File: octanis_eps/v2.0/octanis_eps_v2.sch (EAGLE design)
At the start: 186 parts, among them Q1 CSD16327Q3_DQG_8, Q2 CSD16327Q3_DQG_8, Q3 CSD16327Q3_DQG_8, Q4 BSS123, Q5 CSD16327Q3_DQG_8, Q6 CSD16327Q3_DQG_8, Q7 BSC0901NS, U1 MSP430FR5969, U10 INA213, U11 MIC5019, U12 TPS61088, U13 TPS61232, U15 Value, U16 Value, U17 Value, U2 OPA2333DGK, U3 TPS2022D, U4 TPS2022D, U5 BQ24650_RVA_16, U7 TPS61232, U9 INA213, X1 32.768kHz

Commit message: EPS v2.0 finished routing
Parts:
- removed VCC_GND: (no value), Headerlibrary:PINHD-1X2
- added JP7: (no value), Headerlibrary:PINHD-1X16
- added U$2: UX60SC-MB-5ST, usbminib:UX60SC-MB-5ST
- C31, C47: device rcl:C-EUC0603 -> resistor:C-EUC0805
- JP4: device pinhead:PINHD-2X10 -> Headerlibrary:PINHD-1X6
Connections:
- net +12V: now also JP7.14; no longer JP4.4
- net +3V3: now also JP7.2; no longer VCC_GND.1
- net +3V3_1: now also JP7.6; no longer JP4.12
- net +3V3_2: now also JP7.8; no longer JP4.14
- net +3V3_M: now also JP7.4; no longer JP4.10
- net +5V_1: now also JP7.10; no longer JP4.6
- net +5V_2: now also JP7.12; no longer JP4.8
- net BAT_OUT: now also JP4.1, JP4.3, JP4.5; no longer JP4.15, JP4.17, JP4.19
- net DIRECT: now also JP7.16; no longer JP4.2
- net GND: now also JP7.1, JP7.11, JP7.13, JP7.15, JP7.3, JP7.5, JP7.7, JP7.9, U$2.5; no longer JP4.1, JP4.11, JP4.13, JP4.3, JP4.5, JP4.7, JP4.9, VCC_GND.2
- net HEAT1: now also JP4.6; no longer JP4.16
- net HEAT2: now also JP4.4; no longer JP4.18
- net HEAT3: now also JP4.2; no longer JP4.20
- net V_USB: now also U$2.1
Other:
- moved on the sheet: C31, C47

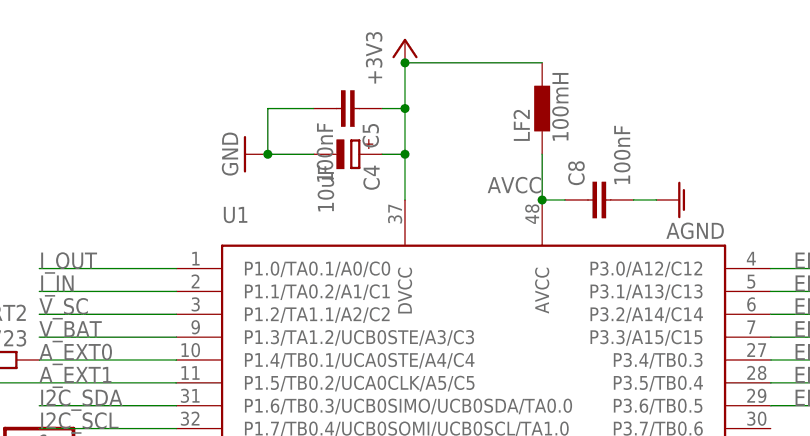
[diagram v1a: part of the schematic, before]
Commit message: performed DRC
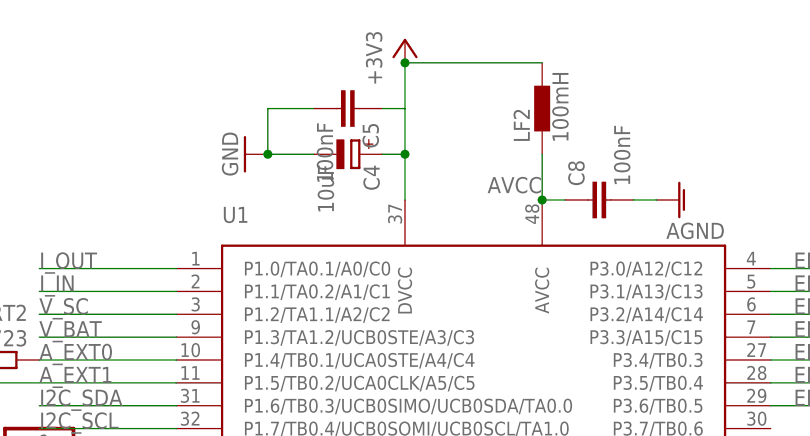
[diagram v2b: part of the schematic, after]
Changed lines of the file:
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@@
 <segment>
 <pinref part="+3V8" gate="G$1" pin="+3V3"/>
-<pinref part="U1" gate="G$1" pin="DVCC"/>
 <wire x1="91.44" y1="307.34" x2="91.44" y2="302.26" width="0.1524" layer="91"/>
 <pinref part="LF2" gate="G$1" pin="2"/>
-<wire x1="91.44" y1="302.26" x2="91.44" y2="297.18" width="0.1524" layer="91"/>
-<wire x1="91.44" y1="297.18" x2="91.44" y2="292.1" width="0.1524" layer="91"/>
 <wire x1="91.44" y1="307.34" x2="106.68" y2="307.34" width="0.1524" layer="91"/>
 <pinref part="C5" gate="G$1" pin="1"/>
 <wire x1="88.9" y1="302.26" x2="91.44" y2="302.26" width="0.1524" layer="91"/>
+<junction x="91.44" y="307.34"/>
+<pinref part="U1" gate="G$1" pin="DVCC"/>
+<wire x1="91.44" y1="292.1" x2="91.44" y2="297.18" width="0.1524" layer="91"/>
 <pinref part="C4" gate="G$1" pin="+"/>
+<wire x1="91.44" y1="297.18" x2="91.44" y2="302.26" width="0.1524" layer="91"/>
 <wire x1="88.9" y1="297.18" x2="91.44" y2="297.18" width="0.1524" layer="91"/>
-<junction x="91.44" y="302.26"/>
-<junction x="91.44" y="307.34"/>
+<junction x="91.44" y="297.18"/>
 </segment>
 <segment>
@@
 <pinref part="C8" gate="G$1" pin="1"/>
 <junction x="106.68" y="292.1"/>
-<junction x="91.44" y="297.18"/>
 <wire x1="109.22" y1="292.1" x2="106.68" y2="292.1" width="0.1524" layer="91"/>
 <label x="106.68" y="294.64" size="1.778" layer="95" rot="R180"/>

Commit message: corrected some GND mistakes; finished v2.0 silk layer
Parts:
- removed J1, J2, J3, J4: (no value), jumper:SJ
- removed RS3: 10m, Octanis1_EPS:CURRENT_RESISTOR
- removed U$1: MCP73831/2, Octanis1_EPS:MCP73831/2
- removed U16: Value, octanis_eps_v05:TPS630250RNCR
- added J108, J109, J110, J111: (no value), jumper:SJ
- added RS2: 10m, Octanis1_EPS:CURRENT_RESISTOR
- added U14: MIC5019, Octanis1_EPS:MIC5019
- added U8: TPS61232, texasinstruments:TPS61232
- C10, C9: value 1.5uF -> 22uF; device rcl:C-EUC0603 -> resistor:C-EUC0805
- C13: value 10uF -> 22uF
- C15: value 22uF -> 10nF; device resistor:C-EUC0805 -> rcl:C-EUC0603
- C16, C18: value 1uF -> 22uF; device rcl:C-EUC0603 -> resistor:C-EUC0805
- C17, C32: value 100nF -> 22uF; device rcl:C-EUC0603 -> resistor:C-EUC0805
- C19: value 10uF -> 10nF; device resistor:C-EUC0805 -> rcl:C-EUC0603
- C20: value 10nF -> 22uF; device rcl:C-EUC0603 -> resistor:C-EUC0805
- C23: value 10uF -> 1uF; device resistor:C-EUC0805 -> rcl:C-EUC0603
- C24, C47: value 22uF -> 100nF; device resistor:C-EUC0805 -> rcl:C-EUC0603
- C25, C39: value 22uF -> 1uF; device resistor:C-EUC0805 -> rcl:C-EUC0603
- C26: value 22uF -> 1.5uF; device resistor:C-EUC0805 -> rcl:C-EUC0603
- C27: value 2.2uF -> 1.5uF
- C28: value 1uF -> 10uF; device rcl:C-EUC0603 -> resistor:C-EUC0805
- C29, C45: value 100nF -> 10uF; device rcl:C-EUC0603 -> resistor:C-EUC0805
- C30: value 22pF -> 10uF; device rcl:C-EUC0603 -> resistor:C-EUC0805
- C34: value 1uF -> 100nF
- C35: value 150pF -> 1uF
- C36: value 22uF -> 22pF; device resistor:C-EUC0805 -> rcl:C-EUC0603
- C37: value 4.7nF -> 10uF; device rcl:C-EUC0603 -> resistor:C-EUC0805
- C38: value 22uF -> 2.2uF; device resistor:C-EUC0805 -> rcl:C-EUC0603
- C40: value 10uF -> 150pF; device resistor:C-EUC0805 -> rcl:C-EUC0603
- C41: value 10uF -> 4.7nF; device resistor:C-EUC0805 -> rcl:C-EUC0603
- C43: value 47uF Tantal -> 10uF; device rcl:C-EUC1210 -> resistor:C-EUC0805
- C44: value 10uF -> 47uF Tantal; device resistor:C-EUC0805 -> rcl:C-EUC1210
- C46: value 47nF -> 100nF
- C48: value 10nF -> 47nF
- JP3: device Headerlibrary:PINHD-1X2 -> Headerlibrary:PINHD-1X16
- JP4: device Headerlibrary:PINHD-1X6 -> Headerlibrary:PINHD-1X2
- JP7: device Headerlibrary:PINHD-1X16 -> Headerlibrary:PINHD-1X6
- L4: value DR127_6u8 -> 1uH; device inductors:DR127 -> Coilcraft:XFL4020
- L6: value 1.5uH -> DR127_6u8; device Coilcraft:XFL4020 -> inductors:DR127
- L7: value 1uH -> 1.5uH
- Q1: value CSD16327Q3_DQG_8 -> BSS123; device texasinstruments:CSD16327Q3_DQG_8 -> transistor-small-signal:BSS123
- Q4: value BSS123 -> CSD16327Q3_DQG_8; device transistor-small-signal:BSS123 -> texasinstruments:CSD16327Q3_DQG_8
- Q6: value CSD16327Q3_DQG_8 -> BSC0901NS; device texasinstruments:CSD16327Q3_DQG_8 -> transistor-power:BSC340N08NS3G
- Q7: value BSC0901NS -> CSD16327Q3_DQG_8; device transistor-power:BSC340N08NS3G -> texasinstruments:CSD16327Q3_DQG_8
- R13, R16: value 1k -> 1.5k
- R17, R19: value 1M -> 100k (0.1%)
- R18: value 1k -> 200k (0.1%)
- R20, R7: value 1k -> 330k (0.1%)
- R21: value 1M -> 150k
- R22, R24: value 1k -> 360k
- R23: value 200k (0.1%) -> 150k
- R25: value 330k (0.1%) -> 150k
- R26: value 1M -> 360k; device resistor:R-EU_R0603 -> rcl:R-EU_R0603
- R27, R53: device resistor:R-EU_R0603 -> rcl:R-EU_R0603
- R28: value dnp -> 1M
- R29: value Rmpph -> 1M
- R30: value 4k7 -> 1M
- R31: value 4k7 -> dnp
- R32: value 1M -> Rmpph
- R33: value Rmppl -> 4k7
- R34: value 100k (1%) -> 4k7
- R35: value 100k (1%) -> 1M
- R36: value 1M -> Rmppl
- R37: value 1M -> 100k (1%)
- R38: value 1M -> 1k; device resistor:R-EU_R0603 -> rcl:R-EU_R0603
- R39: value 2 -> 100k (1%); device rcl:R-EU_R2010 -> rcl:R-EU_R0603
- R4: value 100k (0.1%) -> 1k
- R40: value 10 -> 1k; device rcl:R-EU_R1206 -> rcl:R-EU_R0603
- R41: value 2.2M (1%) -> 1M; device rcl:R-EU_R0603 -> resistor:R-EU_R0603
- R42: device rcl:R-EU_R0603 -> resistor:R-EU_R0603
- R43: value 47k -> 1M
- R44: value 100k -> 2; device resistor:R-EU_R0603 -> rcl:R-EU_R2010
- R45: value 150-220k -> 10; device resistor:R-EU_R0603 -> rcl:R-EU_R1206
- R46: value 56k -> 2.2M (1%); device resistor:R-EU_R0603 -> rcl:R-EU_R0603
- R47: value 430k -> 2k; device resistor:R-EU_R0603 -> rcl:R-EU_R0603
- R48: value dnp -> 470; device resistor:R-EU_R0603 -> rcl:R-EU_R0603
- R49: value 1.5k -> 1k
- R50: value 1M -> 1k
- R52: value 2k -> 1k
- R54: value 470 -> 1k
- R55: value 150k -> 1M
- R56: value 360k -> 1M
- R57: value 360k -> 47k; device rcl:R-EU_R0603 -> resistor:R-EU_R0603
- R58: value 360k -> 100k; device rcl:R-EU_R0603 -> resistor:R-EU_R0603
- R59: value 150k -> 150-220k; device rcl:R-EU_R0603 -> resistor:R-EU_R0603
- R60: value 150k -> 56k; device rcl:R-EU_R0603 -> resistor:R-EU_R0603
- R61: value 1.5k -> 430k; device rcl:R-EU_R0603 -> resistor:R-EU_R0603
- R62: value 1k -> dnp; device rcl:R-EU_R0603 -> resistor:R-EU_R0603
- R8: value 100k (0.1%) -> 1M; device rcl:R-EU_R0603 -> resistor:R-EU_R0603
- R9: value 330k (0.1%) -> 1k
- U10: value INA213 -> BQ24650_RVA_16; device Octanis1_EPS:INA213 -> octanis_eps_v05:BQ24650_RVA_16
- U11: value MIC5019 -> INA213; device Octanis1_EPS:MIC5019 -> Octanis1_EPS:INA213
- U12: value TPS61088 -> INA213; device texasinstruments:TPS61088 -> Octanis1_EPS:INA213
- U13: value TPS61232 -> MCP73831/2; device texasinstruments:TPS61232 -> Octanis1_EPS:MCP73831/2
- U15: value Value -> TPS61088; device octanis_eps_v05:TPS630250RNCR -> texasinstruments:TPS61088
- U4: value TPS2022D -> Value; device Octanis1_EPS:TPS2022D -> octanis_eps_v05:TPS630250RNCR
- U5: value BQ24650_RVA_16 -> Value; device octanis_eps_v05:BQ24650_RVA_16 -> octanis_eps_v05:TPS630250RNCR
- U9: value INA213 -> TPS2022D; device Octanis1_EPS:INA213 -> Octanis1_EPS:TPS2022D
- renumbered U$2 to MINI_USB, U17 to U6
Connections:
- net +12V: now also C49.2, C50.2, C51.2, JP3.14, R61.2, U15.VOUT1, U15.VOUT2, U15.VOUT3; no longer C34.2, C36.2, C38.2, JP7.14, R47.2, U12.VOUT1, U12.VOUT2, U12.VOUT3
- net +3V3: now also C10.1, C9.1, JP3.2, R22.2, R8.2, U4.VOUT, U4.VOUT_2, U4.VOUT_3; no longer C11.1, C12.1, JP7.2, R26.2, R56.2, U15.VOUT, U15.VOUT_2, U15.VOUT_3
- net +3V3_1: now also C11.1, C12.1, JP3.6, R24.2, U5.VOUT, U5.VOUT_2, U5.VOUT_3; no longer C25.1, C26.1, JP7.6, R57.2, U16.VOUT, U16.VOUT_2, U16.VOUT_3
- net +3V3_2: now also C13.1, JP3.8, R26.2; no longer C15.1, JP7.8, R58.2
- net +3V3_M: now also JP3.4; no longer JP7.4
- net +5V_1: now also C16.1, C17.1, C18.1, JP3.10, R28.2; no longer C21.1, C22.1, C24.1, JP7.10, R37.2
- net +5V_2: now also C20.1, C21.1, C22.1, JP3.12, R30.2, U8.FB, U8.VOUT; no longer C49.1, C50.1, C51.1, JP7.12, R51.2, U13.FB, U13.VOUT
- net AGND: now also C26.1, C27.1, R17.1, R19.1, R7.2, U11.GND, U11.REF, U12.GND, U12.REF; no longer C10.1, C9.1, R3.1, R6.1, R9.2, U10.GND, U10.REF, U9.GND, U9.REF
- net AVCC1: now also U11.VCC, U12.VCC; no longer U10.VCC, U9.VCC
- net BAT+: now also C36.1, C37.1, C43.1, R18.2, R39.2, R46.2, RS1.I1, RS2.I2, U13.VBAT; no longer C30.1, C41.1, C42.1, R23.2, R35.2, R41.2, RS1.I2, RS3.I1, U$1.VBAT
- net BAT_11V: now also C47.1, L7.1, Q6G$1.S, U15.EN, U15.VIN; no longer C43.1, L6.1, Q7G$1.S, U12.EN, U12.VIN
- net BAT_OUT: now also C28.1, C29.1, C30.1, C32.1, JP7.1, JP7.3, JP7.5, L4.1, Q6G$1.D, R43.2, RS1.I2, U14.VDD, U4.EN, U4.VIN, U4.VINA, U4.VIN_2, U4.VIN_3, U5.VIN, U5.VINA, U5.VIN_2, U5.VIN_3, U8.VIN, U9.IN1, U9.IN2; no longer C13.1, C19.1, C23.1, C47.1, JP4.1, JP4.3, JP4.5, L7.1, Q7G$1.D, R53.2, RS3.I2, U11.VDD, U13.VIN, U15.EN, U15.VIN, U15.VINA, U15.VIN_2, U15.VIN_3, U16.VIN, U16.VINA, U16.VIN_2, U16.VIN_3, U4.IN1, U4.IN2
- net DIRECT: now also JP3.16, U9.OUT1, U9.OUT2, U9.OUT3; no longer JP7.16, U4.OUT1, U4.OUT2, U4.OUT3
- net EN_12V: now also R56.2, U14.IN; no longer R42.2, U11.IN
- net EN_3V3_1: now also R41.1, U5.EN; no longer R38.1, U16.EN
- net EN_3V3_2: now also R42.1; no longer R27.1
- net EN_3V3_M: now also R8.1; no longer R26.1
- net EN_5V_1: now also R27.2; no longer R36.2
- net EN_5V_2: now also R29.2, U8.EN; no longer R50.2, U13.EN
- net EN_DIRECT: now also R43.1, U9.EN; no longer R53.1, U4.EN
- net EN_HEAT1: now also R50.2, R51.1; no longer R16.2, R17.1
- net EN_HEAT2: now also R52.2, R53.1; no longer R18.2, R19.1
- net EN_HEAT3: now also R54.2, R55.1; no longer R20.2, R21.1
- net EN_SC: now also Q1.G, R31.1, R35.2; no longer Q4.G, R28.1, R32.2
- net GND: now also C10.2, C17.2, C29.2, C30.2, C32.2, C38.2, C40.2, C42.1, C49.1, C50.1, C51.1, C9.2, J100.2, J108.1, J109.1, J110.1, J111.1, JP3.1, JP3.11, JP3.13, JP3.15, JP3.3, JP3.5, JP3.7, JP3.9, Q4.S_2, Q4.S_3, Q5.S, Q5.S_2, Q5.S_3, Q7.S, Q7.S_2, Q7.S_3, R21.1, R23.1, R25.1, R27.1, R29.1, R35.1, R37.1, R41.2, R42.2, R47.2, R51.2, R53.2, R55.2, R56.1, R58.1, R62.2, U10.EPAD, U10.GND, U10.TERM_EN, U13.VSS, U14.GND, U15.AGND, U4.PFM_PWM, U4.PGND, U5.PFM_PWM, U5.PGND, U8.GND, U8.GND1, U8.GND2, U8.GND3, U8.GND4, U8.GND5, U9.GND; no longer C24.2, C26.2, C27.2, C34.1, C36.1, C38.1, C40.1, C42.2, C46.2, C49.2, C50.2, C51.2, J1.1, J102.1, J103.1, J3.1, J4.2, JP7.1, JP7.11, JP7.13, JP7.15, JP7.3, JP7.5, JP7.7, JP7.9, Q1.S_2, Q1.S_3, Q2.S, Q2.S_2, Q2.S_3, Q6.S, Q6.S_2, Q6.S_3, R17.2, R19.2, R21.2, R27.2, R32.1, R33.1, R34.1, R38.2, R42.1, R44.1, R46.1, R48.2, R50.1, R52.2, R55.1, R59.1, U$1.VSS, U11.GND, U12.AGND, U12.PGND, U13.GND, U13.GND1, U13.GND2, U13.GND3, U13.GND4, U13.GND5, U15.GND, U15.PFM_PWM, U16.GND, U16.PFM_PWM, U16.PGND, U5.EPAD, U5.TERM_EN
- net HEAT1: now also JP7.6, Q3.D, Q3.D_2, Q3.D_3, Q3.D_4; no longer JP4.6, Q1.D, Q1.D_2, Q1.D_3, Q1.D_4
- net HEAT2: now also JP7.4, Q4.D, Q4.D_2, Q4.D_3, Q4.D_4; no longer JP4.4, Q2.D, Q2.D_2, Q2.D_3, Q2.D_4
- net HEAT3: now also JP7.2, Q5.D, Q5.D_2, Q5.D_3, Q5.D_4; no longer JP4.2, Q3.D, Q3.D_2, Q3.D_3, Q3.D_4
- net I2C_SCL: now also JP4.2; no longer JP3.2
- net I2C_SDA: now also JP4.1; no longer JP3.1
- net IND: now also L4.2; no longer L5.2
- net IND1: now also L5.2, U8.SW; no longer L7.2, U13.SW
- net I_IN: now also C26.2, R38.1; no longer C9.2, R22.1
- net I_OUT: now also C27.2, R40.1; no longer C10.2, R24.1
- net LED1: now also R14.2; no longer R49.2
- net LED2: now also R16.2; no longer R61.2
- net LED5: now also R13.2; no longer R14.2
- net N$1: now also L1.1, U4.L1; no longer L3.1, U15.L1
- net N$10: now also Q6G$1.G, U14.OUT; no longer Q7G$1.G, U11.OUT
- net N$11: now also L3.1; no longer L1.1
- net N$12: now also L3.2; no longer L1.2
- net N$14: now also J107.2, R13.1; no longer J103.2, R14.1
- net N$19: now also R3.1, R4.2; no longer R4.1, R5.2
- net N$2: now also R28.1; no longer R37.1
- net N$20: now also R3.2; no longer R4.2
- net N$21: now also R17.2, R18.1; no longer R23.1, R3.2
- net N$22: now also R5.2, R6.1; no longer R7.2, R8.1
- net N$23: now also R6.2, R7.1; no longer R8.2, R9.1
- net N$24: now also R19.2, R20.1; no longer R25.1, R6.2
- net N$25: now also R40.2, U11.OUT; no longer R24.2, U10.OUT
- net N$26: now also R38.2, U12.OUT; no longer R22.2, U9.OUT
- net N$27: now also Q5.G, R54.1; no longer Q3.G, R20.1
- net N$3: now also L1.2, U4.L2; no longer L3.2, U15.L2
- net N$31: now also Q4.G, R52.1; no longer Q2.G, R18.1
- net N$32: now also RS1.V1, U11.IN+; no longer RS3.V1, U10.IN+
- net N$33: now also RS1.V2, U11.IN-; no longer RS3.V2, U10.IN-
- net N$34: now also R21.2, R22.1, U4.FB; no longer R55.2, R56.1, U15.FB
- net N$35: now also R23.2, R24.1, U5.FB; no longer R57.1, R59.2, U16.FB
- net N$37: now also Q3.G, R50.1; no longer Q1.G, R16.1
- net N$38: now also C46.2, U15.BOOT; no longer C32.2, U12.BOOT
- net N$39: now also R10.2; no longer R11.2
- net N$4: now also L6.2, RS2.I1; no longer L4.2, RS1.I1
- net N$40: now also J110.2, R10.1; no longer J106.2, R11.1
- net N$42: now also C33.1, R44.1; no longer C27.1, R39.1
- net N$43: now also R9.2; no longer R10.2
- net N$44: now also R30.1, U8.PG; no longer R51.1, U13.PG
- net N$45: now also J111.2, R9.1; no longer J107.2, R10.1
- net N$46: now also R12.2; no longer R13.2
- net N$47: now also J108.2, R12.1; no longer J104.2, R13.1
- net N$49: now also J105.2; no longer J102.2
- net N$5: now also C15.1; no longer C20.1
- net N$50: now also C46.1, L7.2, R57.2, U15.SW1, U15.SW2, U15.SW3, U15.SW4; no longer C32.1, L6.2, R43.2, U12.SW1, U12.SW2, U12.SW3, U12.SW4
- net N$51: now also R11.2; no longer R12.2
- net N$52: now also J109.2, R11.1; no longer J105.2, R12.1
- net N$53: now also R57.1, U15.FSW; no longer R43.1, U12.FSW
- net N$54: now also C41.1, R59.1; no longer C37.1, R45.1
- net N$55: now also J106.2, R14.1; no longer J1.2, R49.1
- net N$56: now also C48.1, U15.SS; no longer C46.1, U12.SS
- net N$57: now also R58.2, U15.ILIM; no longer R44.2, U12.ILIM
- net N$58: now also C40.1, R59.2, U15.COMP; no longer C35.1, R45.2, U12.COMP
- net N$59: now also C38.1, U15.VCC; no longer C33.1, U12.VCC
- net N$6: now also U5.L1; no longer U16.L1
- net N$60: now also R60.2, R61.1, U15.FB; no longer R46.2, R47.1, U12.FB
- net N$61: now also C19.1, U8.SS; no longer C48.1, U13.SS
- net N$62: now also R25.2, R26.1; no longer R58.1, R60.2
- net N$63: now also R47.1, U13.PROG; no longer R52.1, U$1.PROG
- net N$64: now also Q1.D, R32.1, R36.2, U10.MPPSET; no longer Q4.D, R29.1, R33.2, U5.MPPSET
- net N$65: now also J101.1, U13.STAT; no longer J2.1, U$1.STAT
- net N$66: now also R34.1, STAT2.A; no longer R31.1, STAT1.A
- net N$67: now also J103.2, STAT1.C; no longer J101.2, STAT2.C
- net N$68: now also J102.2, STAT2.C; no longer J100.2, STAT1.C
- net N$69: now also R33.1, STAT1.A; no longer R30.1, STAT2.A
- net N$7: now also U5.L2; no longer U16.L2
- net N$70: now also J103.1, U10.STAT2; no longer J101.1, U5.STAT2
- net N$71: now also J102.1, U10.STAT1; no longer J100.1, U5.STAT1
- net N$72: now also C25.1, U10.VREF; no longer C18.1, U5.VREF
- net N$73: now also C35.1, R45.2, U10.VCC; no longer C28.1, R40.2, U5.VCC
- net N$74: now also J101.2, R48.2; no longer J2.2, R54.2
- net N$75: now also R48.1; no longer R54.1
- net N$76: now also C34.1, L6.1, Q2.S, Q2.S_2, Q2.S_3, Q7.D, Q7.D_2, Q7.D_3, Q7.D_4, U10.PH; no longer C29.1, L4.1, Q5.S, Q5.S_2, Q5.S_3, Q6.D, Q6.D_2, Q6.D_3, Q6.D_4, U5.PH
- net N$77: now also J104.2, R16.1; no longer J3.2, R61.1
- net N$78: now also R49.1; no longer R62.1
- net N$79: now also J100.1, R49.2; no longer J4.1, R62.2
- net N$80: now also Q2.G, U10.HIDRV; no longer Q5.G, U5.HIDRV
- net N$81: now also Q7.G, U10.LODRV; no longer Q6.G, U5.LODRV
- net N$82: now also C36.2, R37.2, R39.1, R46.1, U10.VFB; no longer C30.2, R34.2, R35.1, R41.1, U5.VFB
- net N$84: now also C23.1, U10.REGN; no longer C16.1, U5.REGN
- net N$85: now also C34.2, U10.BTST; no longer C29.2, U5.BTST
- net N$9: now also R62.1, U15.MODE; no longer R48.1, U12.MODE
- net SC+: now also C42.2, Q2.D, Q2.D_2, Q2.D_3, Q2.D_4, R20.2, R32.2, R33.2, R34.2, R44.2, R45.1; no longer C40.2, Q5.D, Q5.D_2, Q5.D_3, Q5.D_4, R25.2, R28.2, R29.2, R30.2, R39.2, R40.1
- net TS: now also U10.TS; no longer U5.TS
- net V_BAT: now also R4.1; no longer R5.1
- net V_BAT+: now also C24.1, RS2.V2, U10.SRN, U12.IN-; no longer C17.1, RS1.V2, U5.SRN, U9.IN-
- net V_SC: now also R5.1; no longer R7.1
- net V_SCOUT: now also C24.2, RS2.V1, U10.SRP, U12.IN+; no longer C17.2, RS1.V1, U5.SRP, U9.IN+
- net V_USB: now also U13.VDD; no longer U$1.VDD
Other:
- moved on the sheet: C10, C11, C12, C13, C15, C16, C17, C18, C19, C20, C21, C22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
